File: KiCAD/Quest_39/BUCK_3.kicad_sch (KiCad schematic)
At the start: 21 parts

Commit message: Fixed most ERC errors
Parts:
- gave numbers to parts that had none: 21
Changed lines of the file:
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@@
   (symbol (lib_id "Device:C_Polarized") (at 354.33 171.45 0) (unit 1)
     (in_bom yes) (on_board yes)
-    (property "Reference" "C?" (id 0) (at 358.1195 170.1375 0)
+    (property "Reference" "C72" (id 0) (at 358.1195 170.1375 0)
       (effects (font (size 1.27 1.27)) (justify left))
     )
@@
   (symbol (lib_id "Device:C") (at 335.28 171.45 0) (unit 1)
     (in_bom yes) (on_board yes) (fields_autoplaced)
-    (property "Reference" "C?" (id 0) (at 339.09 170.1799 0)
+    (property "Reference" "C71" (id 0) (at 339.09 170.1799 0)
       (effects (font (size 1.27 1.27)) (justify left))
     )
@@
   (symbol (lib_id "Device:C") (at 337.82 223.52 0) (unit 1)
     (in_bom yes) (on_board yes) (fields_autoplaced)
-    (property "Reference" "C?" (id 0) (at 341.63 222.2499 0)
+    (property "Reference" "C76" (id 0) (at 341.63 222.2499 0)
       (effects (font (size 1.27 1.27)) (justify left))
     )
@@
   (symbol (lib_id "Device:R") (at 60.96 48.26 0) (unit 1)
     (in_bom yes) (on_board yes) (fields_autoplaced)
-    (property "Reference" "R?" (id 0) (at 63.5 46.9899 0)
+    (property "Reference" "R30" (id 0) (at 63.5 46.9899 0)
       (effects (font (size 1.27 1.27)) (justify left))
     )
@@
   (symbol (lib_id "Device:R") (at 322.58 214.63 0) (unit 1)
     (in_bom yes) (on_board yes) (fields_autoplaced)
-    (property "Reference" "R?" (id 0) (at 325.12 213.3599 0)
+    (property "Reference" "R32" (id 0) (at 325.12 213.3599 0)
       (effects (font (size 1.27 1.27)) (justify left))
     )
@@
   (symbol (lib_id "Device:R") (at 55.88 40.64 90) (unit 1)
     (in_bom yes) (on_board yes) (fields_autoplaced)
-    (property "Reference" "R?" (id 0) (at 55.88 34.29 90))
+    (property "Reference" "R28" (id 0) (at 55.88 34.29 90))
     (property "Value" "0R0025" (id 1) (at 55.88 36.83 90))
     (property "Footprint" "" (id 2) (at 55.88 42.418 90)
@@
   (symbol (lib_id "Amplifier_Operational:MCP601-xOT") (at 35.56 64.77 0) (unit 1)
     (in_bom yes) (on_board yes)
-    (property "Reference" "U?" (id 0) (at 38.1 60.96 0))
+    (property "Reference" "U20" (id 0) (at 38.1 60.96 0))
     (property "Value" "MCP601T-I/OT" (id 1) (at 41.91 68.58 0))
     (property "Footprint" "Package_TO_SOT_SMD:SOT-23-5" (id 2) (at 33.02 69.85 0)
@@
   (symbol (lib_id "Device:C") (at 125.73 45.72 0) (unit 1)
     (in_bom yes) (on_board yes) (fields_autoplaced)
-    (property "Reference" "C?" (id 0) (at 129.54 44.4499 0)
+    (property "Reference" "C68" (id 0) (at 129.54 44.4499 0)
       (effects (font (size 1.27 1.27)) (justify left))
     )
@@
   (symbol (lib_id "Device:R") (at 48.26 48.26 0) (unit 1)
     (in_bom yes) (on_board yes) (fields_autoplaced)
-    (property "Reference" "R?" (id 0) (at 50.8 46.9899 0)
+    (property "Reference" "R29" (id 0) (at 50.8 46.9899 0)
       (effects (font (size 1.27 1.27)) (justify left))
     )
@@
   (symbol (lib_id "Device:C_Polarized") (at 381 171.45 0) (unit 1)
     (in_bom yes) (on_board yes)
-    (property "Reference" "C?" (id 0) (at 384.7895 170.1375 0)
+    (property "Reference" "C74" (id 0) (at 384.7895 170.1375 0)
       (effects (font (size 1.27 1.27)) (justify left))
     )
@@
   (symbol (lib_id "Device:C") (at 100.33 45.72 0) (unit 1)
     (in_bom yes) (on_board yes) (fields_autoplaced)
-    (property "Reference" "C?" (id 0) (at 104.14 44.4499 0)
+    (property "Reference" "C66" (id 0) (at 104.14 44.4499 0)
       (effects (font (size 1.27 1.27)) (justify left))
     )
@@
   (symbol (lib_id "Device:C_Polarized") (at 368.3 171.45 0) (unit 1)
     (in_bom yes) (on_board yes)
-    (property "Reference" "C?" (id 0) (at 372.0895 170.1375 0)
+    (property "Reference" "C73" (id 0) (at 372.0895 170.1375 0)
       (effects (font (size 1.27 1.27)) (justify left))
     )
@@
   (symbol (lib_id "Device:C_Polarized") (at 393.7 171.45 0) (unit 1)
     (in_bom yes) (on_board yes)
-    (property "Reference" "C?" (id 0) (at 397.4895 170.1375 0)
+    (property "Reference" "C75" (id 0) (at 397.4895 170.1375 0)
       (effects (font (size 1.27 1.27)) (justify left))
     )
@@
   (symbol (lib_id "Device:C") (at 55.88 54.61 90) (unit 1)
     (in_bom yes) (on_board yes)
-    (property "Reference" "C?" (id 0) (at 55.88 50.8 90))
+    (property "Reference" "C69" (id 0) (at 55.88 50.8 90))
     (property "Value" "1uF" (id 1) (at 55.88 58.42 90))
     (property "Footprint" "OptoDevice:R_LDR_4.9x4.2mm_P2.54mm_Vertical" (id 2) (at 59.69 53.6448 0)
@@
   (symbol (lib_id "Device:C_Polarized") (at 86.36 45.72 0) (unit 1)
     (in_bom yes) (on_board yes) (fields_autoplaced)
-    (property "Reference" "C?" (id 0) (at 90.17 43.5609 0)
+    (property "Reference" "C65" (id 0) (at 90.17 43.5609 0)
       (effects (font (size 1.27 1.27)) (justify left))
     )
@@
   (symbol (lib_id "LTM4611EV:LTM4611EV-PBF") (at 132.08 101.6 0) (unit 1)
     (in_bom yes) (on_board yes)
-    (property "Reference" "U?" (id 0) (at 308.61 49.53 0)
+    (property "Reference" "U22" (id 0) (at 308.61 49.53 0)
       (effects (font (size 1.524 1.524)))
     )
@@
   (symbol (lib_id "Analog_ADC:INA226") (at 78.74 72.39 0) (unit 1)
     (in_bom yes) (on_board yes)
-    (property "Reference" "U?" (id 0) (at 83.82 60.96 0)
+    (property "Reference" "U21" (id 0) (at 83.82 60.96 0)
       (effects (font (size 1.27 1.27)) (justify left))
     )
@@
   (symbol (lib_id "Device:R") (at 127 90.17 0) (unit 1)
     (in_bom yes) (on_board yes) (fields_autoplaced)
-    (property "Reference" "R?" (id 0) (at 129.54 88.8999 0)
+    (property "Reference" "R31" (id 0) (at 129.54 88.8999 0)
       (effects (font (size 1.27 1.27)) (justify left))
     )
@@
   (symbol (lib_id "Device:C") (at 113.03 45.72 0) (unit 1)
     (in_bom yes) (on_board yes) (fields_autoplaced)
-    (property "Reference" "C?" (id 0) (at 116.84 44.4499 0)
+    (property "Reference" "C67" (id 0) (at 116.84 44.4499 0)
       (effects (font (size 1.27 1.27)) (justify left))
     )
@@
   (symbol (lib_id "MCP4151:MCP4151-502E{slash}SN") (at 254 219.71 0) (unit 1)
     (in_bom yes) (on_board yes)
-    (property "Reference" "U?" (id 0) (at 312.42 213.36 0)
+    (property "Reference" "U23" (id 0) (at 312.42 213.36 0)
       (effects (font (size 1.524 1.524)))
     )
@@
   (symbol (lib_id "Device:C") (at 128.27 135.89 0) (unit 1)
     (in_bom yes) (on_board yes) (fields_autoplaced)
-    (property "Reference" "C?" (id 0) (at 132.08 134.6199 0)
-      (effects (font (size 1.27 1.27)) (justify left))
-    )
+    (property "Reference" "C70" (id 0) (at 132.08 134.6199 0)
+      (effects (font (size 1.27 1.27)) (justify left))
+    )

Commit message: Gave all INA226's unique addresses
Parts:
- removed C65: 330uF, symbol Device:C_Polarized
- removed C66, C67, C68: 22uF, symbol Device:C
- removed C69: 1uF, OptoDevice:R_LDR_4.9x4.2mm_P2.54mm_Vertical, symbol Device:C
- removed C70: 100nF, symbol Device:C
- removed C72, C73, C74, C75: 100uF, symbol Device:C_Polarized
- removed R28: 0R0025, symbol Device:R
- removed R29, R30: 10, symbol Device:R
- removed R31: 10K, symbol Device:R
- removed R32: 20K, symbol Device:R
- removed U20: MCP601T-I/OT, Package_TO_SOT_SMD:SOT-23-5, symbol Amplifier_Operational:MCP601-xOT
- added C70: 330uF, symbol Device:C_Polarized
- added C72, C73: 22uF, symbol Device:C
- added C74: 1uF, OptoDevice:R_LDR_4.9x4.2mm_P2.54mm_Vertical, symbol Device:C
- added C75, C83: 100nF, symbol Device:C
- added C77: 10nF, symbol Device:C
- added C78, C79, C80, C81: 100uF, symbol Device:C_Polarized
- added C82: 100pF, symbol Device:C
- added R45: 0R0025, symbol Device:R
- added R46, R47: 10R, symbol Device:R
- added R48: 9k, symbol Device:R
- added R49: 1k, symbol Device:R
- added R50: 10k, symbol Device:R
- added R51: 20K, symbol Device:R
- added TP34, TP35, TP36, TP37, TP38, TP39, TP40: TestPoint, symbol Connector:TestPoint
- added U20: AD626ANZ, N_8_ADI, symbol AD626ANZ:AD626ANZ
- C71: value 100pF -> 22uF
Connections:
- net +5V: now also C83.1, U20.6 (+VS)
- net GND: now also C75.2, C83.2, U20.2 (AGND), U20.3 (-VS); no longer U21.2 (A0), U21.3 (~{Alert})
- net NEG: now also C71.2, C70.2, C72.2, C73.2, C77.1, C78.2, C79.2, C80.2, C81.2, R49.2, U20.1 (-IN); no longer U21.8 (Vbus)
- net P0A: now also R51.2
- net POS: now also C78.1, C79.1, C80.1, C81.1, C82.1; no longer C71.1
- net PV_POS: now also C71.1, U22.A1 (VIN), U22.A2 (VIN), U22.A3 (VIN), U22.A4 (VIN), U22.A5 (VIN), U22.A6 (VIN), U22.B1 (VIN), U22.B2 (VIN), U22.B3 (VIN), U22.B4 (VIN), U22.B5 (VIN), U22.B6 (VIN), U22.C1 (VIN), U22.C2 (VIN), U22.C3 (VIN), U22.C4 (VIN), U22.C5 (VIN), U22.C6 (VIN), C70.1, C72.1, C73.1, R45.1, R45.2, R46.1, R47.1, R48.1, R50.1
- net RUN: now also R50.2
- net SCL: now also U21.2 (A0)
- net TRACK/SS: now also C77.2
- net Vfb: now also C82.2, R51.1; no longer C71.2
- net Vin+: now also C74.1, R46.2
- net Vin-: now also U21.8 (Vbus), U21.9 (Vin-), C74.2, R47.2, TP35.1, U20.5 (OUT)
- net at U22.A11 (COMP): now also TP38.1
- net at U22.A7 (INTVCC): now also U22.D9 (INTVCC), TP34.1
- net at U22.B12 (PLLFLTR/FSET): now also TP37.1
- net at U22.F11 (PGOOD): now also U22.G12 (PGOOD), TP36.1
- net at U22.K12 (DIFFVOUT), U22.L12 (VOUT_LCL): now also TP39.1, TP40.1
- new net: C75.1, U20.4 (FILTER)
- new net +IN: R48.2, R49.1, U20.8 (+IN)
- no-connect marks 16 -> 12
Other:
- note added: "10:1 divider"
- note added: "Addr=0x43"
- note added: "Extra mounting"
- note added: "G=10"
- note added: "Output voltage is set by varying Rfb with a digipot. SPI = 00"
- note added: "the measured voltage is divided and then amplified by 10 as to simulate a follower. This is done to make use of the AD626 (low price and availability)."

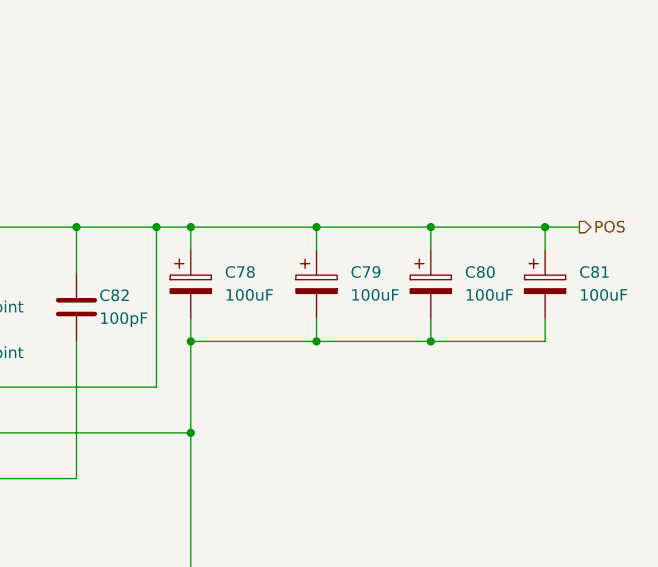
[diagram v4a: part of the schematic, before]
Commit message: Assigned all schem. symbols their footprints
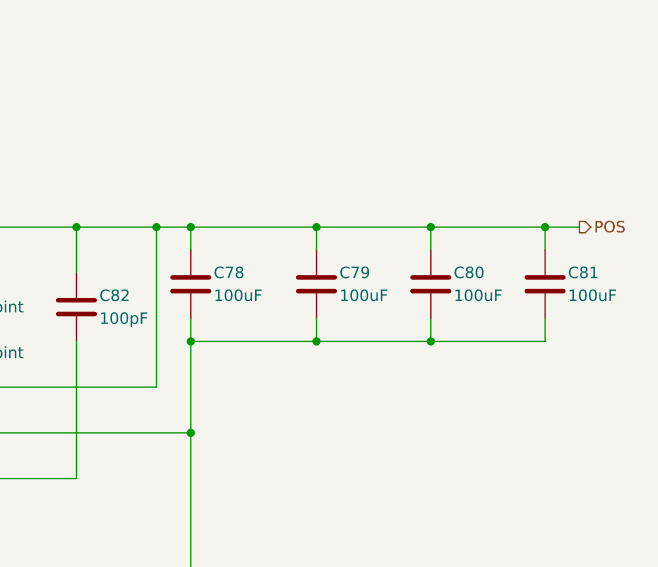
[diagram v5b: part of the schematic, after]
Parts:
- removed C78, C79, C80, C81: 100uF, symbol Device:C_Polarized
- added C78, C79, C80, C81: 100uF, Capacitor_SMD:C_1206_3216Metric, symbol Device:C
- C70: footprint (none) -> Capacitor_SMD:CP_Elec_8x6.9
- C71, C72, C73, C75, C76, C77, C82, C83: footprint (none) -> Capacitor_SMD:C_0805_2012Metric
- C74: footprint OptoDevice:R_LDR_4.9x4.2mm_P2.54mm_Vertical -> Capacitor_SMD:C_0805_2012Metric
- R45: footprint (none) -> Resistor_SMD:R_1206_3216Metric
- R46, R47, R48, R49, R50, R51: footprint (none) -> Resistor_SMD:R_0805_2012Metric
- TP34, TP35, TP36, TP37, TP38, TP39, TP40: footprint (none) -> TestPoint:TestPoint_Pad_D2.0mm
- U20: footprint N_8_ADI -> Package_DIP:DIP-8_W7.62mm_Socket_LongPads
- U22: footprint LGA-133_3_LIT -> Package_LGA:Linear_LGA-133_15.0x15.0mm_Layout12x12_P1.27mm
- U23: footprint SOIC8-N_MC_MCH -> Package_SO:MSOP-8_3x3mm_P0.65mm
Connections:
- net NEG: now also C78.2, C79.2, C80.2, C81.2
- net POS: now also C78.1, C79.1, C80.1, C81.1

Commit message: Initial work on layout
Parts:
- C74, C75, C76, C77, C82, C83: footprint Capacitor_SMD:C_0805_2012Metric -> Capacitor_SMD:C_0603_1608Metric
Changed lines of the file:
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@@
       (effects (font (size 1.27 1.27)) (justify left))
     )
-    (property "Footprint" "Capacitor_SMD:C_0805_2012Metric" (id 2) (at 106.3752 127 0)
+    (property "Footprint" "Capacitor_SMD:C_0603_1608Metric" (id 2) (at 106.3752 127 0)
       (effects (font (size 1.27 1.27)) hide)
     )
@@
       (effects (font (size 1.27 1.27)) (justify left))
     )
-    (property "Footprint" "Capacitor_SMD:C_0805_2012Metric" (id 2) (at 64.4652 85.09 0)
+    (property "Footprint" "Capacitor_SMD:C_0603_1608Metric" (id 2) (at 64.4652 85.09 0)
       (effects (font (size 1.27 1.27)) hide)
     )
@@
       (effects (font (size 1.27 1.27)) (justify left))
     )
-    (property "Footprint" "Capacitor_SMD:C_0805_2012Metric" (id 2) (at 341.3252 223.52 0)
+    (property "Footprint" "Capacitor_SMD:C_0603_1608Metric" (id 2) (at 341.3252 223.52 0)
       (effects (font (size 1.27 1.27)) hide)
     )
@@
       (effects (font (size 1.27 1.27)) (justify left))
     )
-    (property "Footprint" "Capacitor_SMD:C_0805_2012Metric" (id 2) (at 345.1352 171.45 0)
+    (property "Footprint" "Capacitor_SMD:C_0603_1608Metric" (id 2) (at 345.1352 171.45 0)
       (effects (font (size 1.27 1.27)) hide)
     )
@@
       (effects (font (size 1.27 1.27)) (justify left))
     )
-    (property "Footprint" "Capacitor_SMD:C_0805_2012Metric" (id 2) (at 26.3652 83.82 0)
+    (property "Footprint" "Capacitor_SMD:C_0603_1608Metric" (id 2) (at 26.3652 83.82 0)
       (effects (font (size 1.27 1.27)) hide)
     )
@@
     (property "Reference" "C74" (id 0) (at 74.93 59.69 90))
     (property "Value" "1uF" (id 1) (at 74.93 67.31 90))
-    (property "Footprint" "Capacitor_SMD:C_0805_2012Metric" (id 2) (at 78.74 62.5348 0)
-      (effects (font (size 1.27 1.27)) hide)
-    )
+    (property "Footprint" "Capacitor_SMD:C_0603_1608Metric" (id 2) (at 78.74 62.5348 0)
+      (effects (font (size 1.27 1.27)) hide)
+    )

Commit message: Fixed INA226 schem. mistake and further layout work
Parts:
- added C79: 100nF, Capacitor_SMD:C_0603_1608Metric, symbol Device:C
- renumbered C70 to C74, C71 to C75, C72 to C76, C73 to C77, C74 to C78, C75 to C80, C76 to C81, C77 to C82, C78 to C83, C79 to C84, C80 to C85, C81 to C86, C82 to C87, C83 to C88
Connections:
- net +5V: now also C79.1
- net GND: now also C79.2
- net PV_POS: no longer C74.1, C75.1, C76.1, C77.1, R45.2, R47.1, R50.1, U22.A1 (VIN), U22.A2 (VIN), U22.A3 (VIN), U22.A4 (VIN), U22.A5 (VIN), U22.A6 (VIN), U22.B1 (VIN), U22.B2 (VIN), U22.B3 (VIN), U22.B4 (VIN), U22.B5 (VIN), U22.B6 (VIN), U22.C1 (VIN), U22.C2 (VIN), U22.C3 (VIN), U22.C4 (VIN), U22.C5 (VIN), U22.C6 (VIN)
- net Vin-: no longer TP35.1, U20.5 (OUT), U21.8 (Vbus)
- new net: TP35.1, U20.5 (OUT), U21.8 (Vbus)
- new net BUCK_VIN: C74.1, C75.1, C76.1, C77.1, R45.2, R47.1, R50.1, U22.A1 (VIN), U22.A2 (VIN), U22.A3 (VIN), U22.A4 (VIN), U22.A5 (VIN), U22.A6 (VIN), U22.B1 (VIN), U22.B2 (VIN), U22.B3 (VIN), U22.B4 (VIN), U22.B5 (VIN), U22.B6 (VIN), U22.C1 (VIN), U22.C2 (VIN), U22.C3 (VIN), U22.C4 (VIN), U22.C5 (VIN), U22.C6 (VIN)

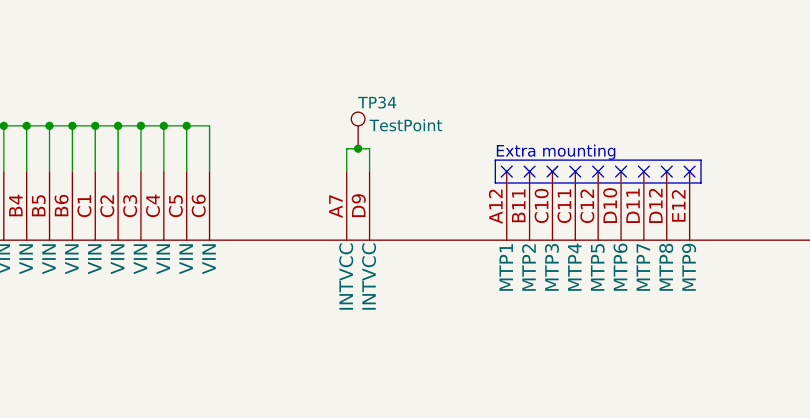
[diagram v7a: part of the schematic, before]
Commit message: Partial wiring of first buck converter section PCB layout
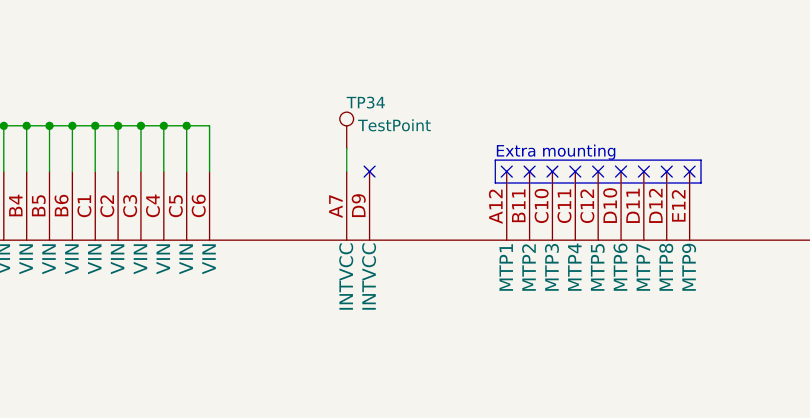
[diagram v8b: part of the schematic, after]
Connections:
- net at TP34.1, U22.A7 (INTVCC): no longer U22.D9 (INTVCC)
- no-connect marks 12 -> 13
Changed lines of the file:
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@@
   (junction (at 322.58 87.63) (diameter 0) (color 0 0 0 0)
   )
-  (junction (at 234.95 39.37) (diameter 0) (color 0 0 0 0)
-  )
   (junction (at 130.81 36.83) (diameter 0) (color 0 0 0 0)
   )
@@
   (junction (at 356.87 171.45) (diameter 0) (color 0 0 0 0)
   )
+  (no_connect (at 236.22 41.91))
   (no_connect (at 256.54 41.91))
   (no_connect (at 271.78 41.91))
@@
     (stroke (width 0) (type default) (color 0 0 0 0))
   )
-  (wire (pts (xy 236.22 39.37) (xy 236.22 41.91))
-    (stroke (width 0) (type default) (color 0 0 0 0))
-  )
   (wire (pts (xy 67.31 63.5) (xy 67.31 53.34))
     (stroke (width 0) (type default) (color 0 0 0 0))
@@
     (stroke (width 0) (type default) (color 0 0 0 0))
   )
-  (wire (pts (xy 233.68 39.37) (xy 234.95 39.37))
-    (stroke (width 0) (type default) (color 0 0 0 0))
-  )
   (wire (pts (xy 82.55 53.34) (xy 82.55 63.5))
     (stroke (width 0) (type default) (color 0 0 0 0))
@@
     (stroke (width 0) (type default) (color 0 0 0 0))
   )
+  (wire (pts (xy 233.68 41.91) (xy 233.68 39.37))
+    (stroke (width 0) (type default) (color 0 0 0 0))
+  )
   (wire (pts (xy 325.12 186.69) (xy 322.58 186.69))
     (stroke (width 0) (type default) (color 0 0 0 0))
@@
     (stroke (width 0) (type default) (color 0 0 0 0))
   )
-  (wire (pts (xy 234.95 39.37) (xy 236.22 39.37))
-    (stroke (width 0) (type default) (color 0 0 0 0))
-  )
   (wire (pts (xy 215.9 36.83) (xy 218.44 36.83))
     (stroke (width 0) (type default) (color 0 0 0 0))
@@
   )
   (wire (pts (xy 130.81 36.83) (xy 130.81 38.1))
-    (stroke (width 0) (type default) (color 0 0 0 0))
-  )
-  (wire (pts (xy 233.68 41.91) (xy 233.68 39.37))
     (stroke (width 0) (type default) (color 0 0 0 0))
   )
@@
     (pin "1")
   )
-  (symbol (lib_id "Connector:TestPoint") (at 234.95 39.37 0) (unit 1)
-    (in_bom yes) (on_board yes)
-    (property "Reference" "TP34" (id 0) (at 234.95 34.29 0)
-      (effects (font (size 1.27 1.27)) (justify left))
-    )
-    (property "Value" "TestPoint" (id 1) (at 236.22 36.83 0)
-      (effects (font (size 1.27 1.27)) (justify left))
-    )
-    (property "Footprint" "TestPoint:TestPoint_Pad_D2.0mm" (id 2) (at 240.03 39.37 0)
-      (effects (font (size 1.27 1.27)) hide)
-    )
-    (property "Datasheet" "~" (id 3) (at 240.03 39.37 0)
-      (effects (font (size 1.27 1.27)) hide)
-    )
-    (pin "1")
-  )
   (symbol (lib_id "power:GND") (at 21.59 72.39 0) (unit 1)
     (in_bom yes) (on_board yes)
@@
     (pin "2")
   )
+  (symbol (lib_id "Connector:TestPoint") (at 233.68 39.37 0) (unit 1)
+    (in_bom yes) (on_board yes)
+    (property "Reference" "TP34" (id 0) (at 233.68 34.29 0)
+      (effects (font (size 1.27 1.27)) (justify left))
+    )
+    (property "Value" "TestPoint" (id 1) (at 234.95 36.83 0)
+      (effects (font (size 1.27 1.27)) (justify left))
+    )
+    (property "Footprint" "TestPoint:TestPoint_Pad_D2.0mm" (id 2) (at 238.76 39.37 0)
+      (effects (font (size 1.27 1.27)) hide)
+    )
+    (property "Datasheet" "~" (id 3) (at 238.76 39.37 0)
+      (effects (font (size 1.27 1.27)) hide)
+    )
+    (pin "1")
+  )
   (symbol (lib_id "power:+5V") (at 64.77 69.85 0) (unit 1)
